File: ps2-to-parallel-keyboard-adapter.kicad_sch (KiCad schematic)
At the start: 7 parts, among them J1 PS/2 Keyboard Mini DIN 6, J2 Ferguson Keyboard Connector J2, U1 PIC16F84A, Y1 4 MHz

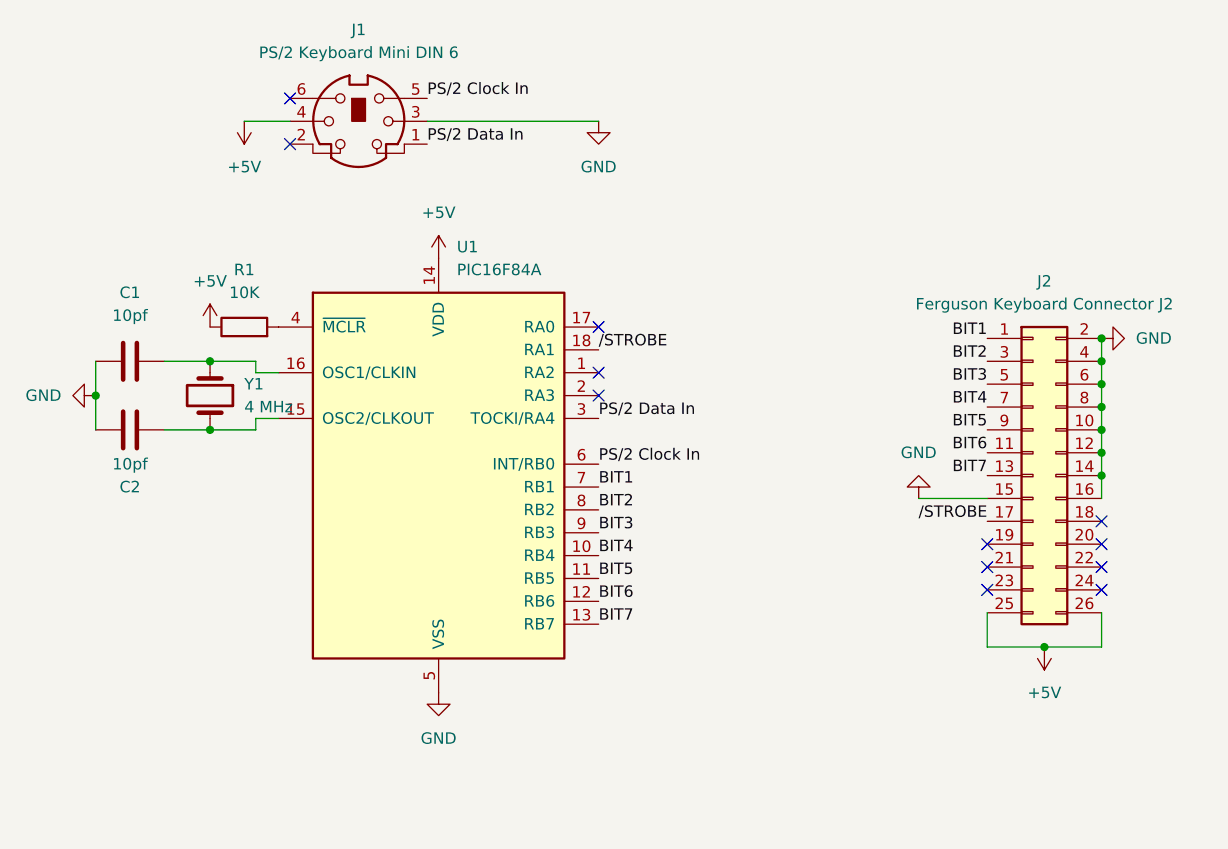
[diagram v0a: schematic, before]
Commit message: v1.1, add decoupling cap
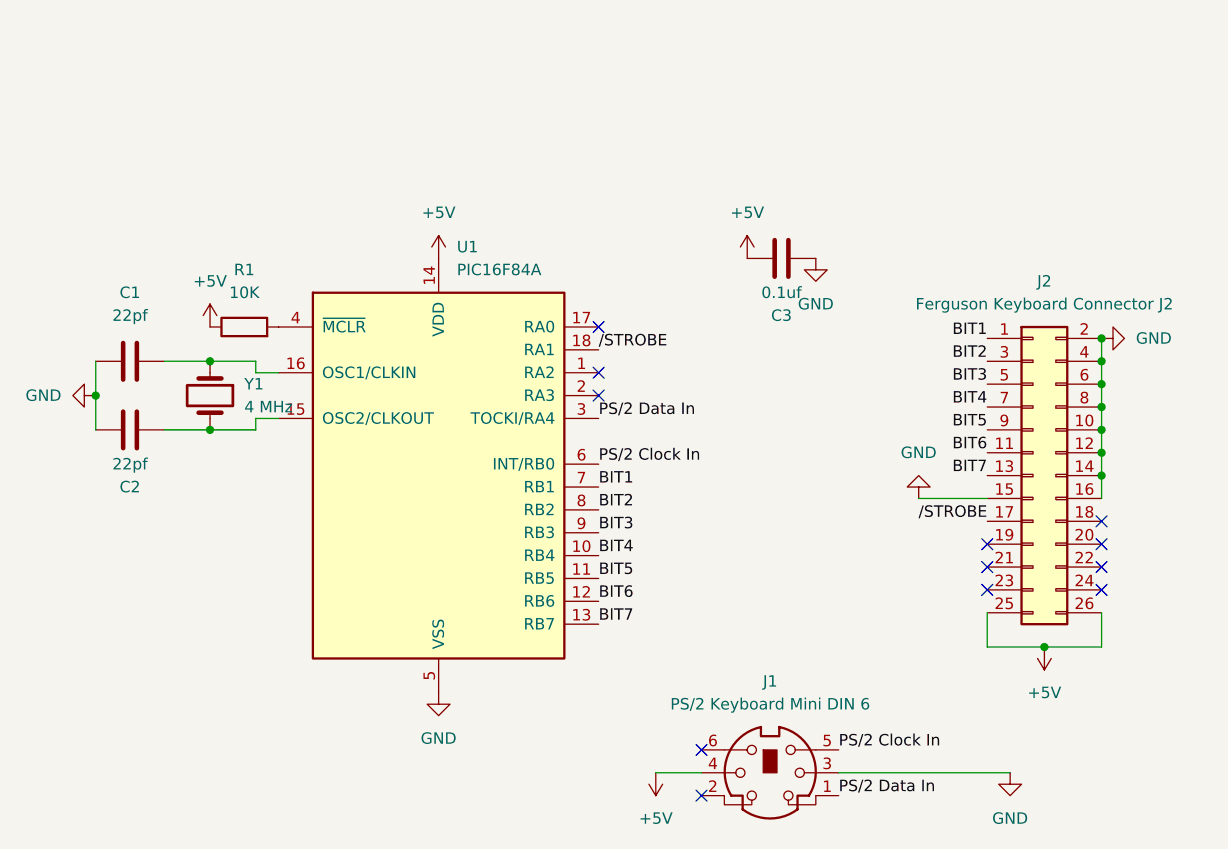
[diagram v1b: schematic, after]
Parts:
- added C3: 0.1uf, Capacitor_THT:C_Rect_L4.0mm_W2.5mm_P2.50mm, symbol Device:C
- C1, C2: value 10pf -> 22pf
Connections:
- net +5V: now also C3.1
- net GND: now also C3.2
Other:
- moved on the sheet: J1
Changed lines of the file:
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@@
   (no_connect (at 214.63 100.33))
   (no_connect (at 214.63 97.79))
-  (no_connect (at 137.16 53.34))
+  (no_connect (at 182.88 125.73))
   (no_connect (at 171.45 81.28))
   (no_connect (at 227.33 95.25))
@@
   (no_connect (at 227.33 102.87))
   (no_connect (at 227.33 97.79))
-  (no_connect (at 137.16 48.26))
+  (no_connect (at 182.88 120.65))
   (no_connect (at 171.45 73.66))
   (wire (pts (xy 133.35 85.09) (xy 128.27 85.09))
@@
     (stroke (width 0) (type default) (color 0 0 0 0))
   )
-  (wire (pts (xy 152.4 50.8) (xy 171.45 50.8))
+  (wire (pts (xy 198.12 123.19) (xy 217.17 123.19))
     (stroke (width 0) (type default) (color 0 0 0 0))
   )
@@
     (stroke (width 0) (type default) (color 0 0 0 0))
   )
-  (wire (pts (xy 132.08 50.8) (xy 137.16 50.8))
+  (wire (pts (xy 177.8 123.19) (xy 182.88 123.19))
     (stroke (width 0) (type default) (color 0 0 0 0))
   )
@@
     (effects (font (size 1.27 1.27)) (justify left bottom))
   )
-  (label "PS{slash}2 Clock In" (at 152.4 48.26 0)
+  (label "PS{slash}2 Clock In" (at 198.12 120.65 0)
     (effects (font (size 1.27 1.27)) (justify left bottom))
   )
@@
     (effects (font (size 1.27 1.27)) (justify right bottom))
   )
-  (label "PS{slash}2 Data In" (at 152.4 53.34 0)
+  (label "PS{slash}2 Data In" (at 198.12 125.73 0)
     (effects (font (size 1.27 1.27)) (justify left bottom))
   )
@@
     (pin "9")
   )
+  (symbol (lib_id "power:+5V") (at 187.96 66.04 0) (unit 1)
+    (in_bom yes) (on_board yes) (fields_autoplaced)
+    (property "Reference" "#PWR01" (id 0) (at 187.96 69.85 0)
+      (effects (font (size 1.27 1.27)) hide)
+    )
+    (property "Value" "+5V" (id 1) (at 187.96 60.96 0))
+    (property "Footprint" "" (id 2) (at 187.96 66.04 0)
+      (effects (font (size 1.27 1.27)) hide)
+    )
+    (property "Datasheet" "" (id 3) (at 187.96 66.04 0)
+      (effects (font (size 1.27 1.27)) hide)
+    )
+    (pin "1")
+  )
   (symbol (lib_id "Device:C") (at 119.38 85.09 90) (unit 1)
     (in_bom yes) (on_board yes)
     (property "Reference" "C2" (id 0) (at 119.38 91.44 90))
-    (property "Value" "10pf" (id 1) (at 119.38 88.9 90))
+    (property "Value" "22pf" (id 1) (at 119.38 88.9 90))
     (property "Footprint" "Capacitor_THT:C_Rect_L4.0mm_W2.5mm_P2.50mm" (id 2) (at 123.19 84.1248 0)
       (effects (font (size 1.27 1.27)) hide)
@@
     (pin "1")
   )
+  (symbol (lib_id "Device:C") (at 191.77 66.04 90) (unit 1)
+    (in_bom yes) (on_board yes)
+    (property "Reference" "C3" (id 0) (at 191.77 72.39 90))
+    (property "Value" "0.1uf" (id 1) (at 191.77 69.85 90))
+    (property "Footprint" "Capacitor_THT:C_Rect_L4.0mm_W2.5mm_P2.50mm" (id 2) (at 195.58 65.0748 0)
+      (effects (font (size 1.27 1.27)) hide)
+    )
+    (property "Datasheet" "~" (id 3) (at 191.77 66.04 0)
+      (effects (font (size 1.27 1.27)) hide)
+    )
+    (pin "1")
+    (pin "2")
+  )
   (symbol (lib_id "Device:C") (at 119.38 77.47 90) (unit 1)
     (in_bom yes) (on_board yes) (fields_autoplaced)
     (property "Reference" "C1" (id 0) (at 119.38 69.85 90))
-    (property "Value" "10pf" (id 1) (at 119.38 72.39 90))
+    (property "Value" "22pf" (id 1) (at 119.38 72.39 90))
     (property "Footprint" "Capacitor_THT:C_Rect_L4.0mm_W2.5mm_P2.50mm" (id 2) (at 123.19 76.5048 0)
       (effects (font (size 1.27 1.27)) hide)
@@
     (pin "9")
   )
-  (symbol (lib_id "Connector:Mini-DIN-6") (at 144.78 50.8 0) (unit 1)
-    (in_bom yes) (on_board yes) (fields_autoplaced)
-    (property "Reference" "J1" (id 0) (at 144.7977 40.64 0))
-    (property "Value" "PS/2 Keyboard Mini DIN 6" (id 1) (at 144.7977 43.18 0))
-    (property "Footprint" "SnapEDA Library:CUI_MD-60SM" (id 2) (at 144.78 50.8 0)
-      (effects (font (size 1.27 1.27)) hide)
-    )
-    (property "Datasheet" "http://service.powerdynamics.com/ec/Catalog17/Section%2011.pdf" (id 3) (at 144.78 50.8 0)
+  (symbol (lib_id "Connector:Mini-DIN-6") (at 190.5 123.19 0) (unit 1)
+    (in_bom yes) (on_board yes) (fields_autoplaced)
+    (property "Reference" "J1" (id 0) (at 190.5177 113.03 0))
+    (property "Value" "PS/2 Keyboard Mini DIN 6" (id 1) (at 190.5177 115.57 0))
+    (property "Footprint" "SnapEDA Library:CUI_MD-60SM" (id 2) (at 190.5 123.19 0)
+      (effects (font (size 1.27 1.27)) hide)
+    )
+    (property "Datasheet" "http://service.powerdynamics.com/ec/Catalog17/Section%2011.pdf" (id 3) (at 190.5 123.19 0)
       (effects (font (size 1.27 1.27)) hide)
     )
@@
     (pin "6")
   )
-  (symbol (lib_id "power:+5V") (at 132.08 50.8 180) (unit 1)
-    (in_bom yes) (on_board yes) (fields_autoplaced)
-    (property "Reference" "#PWR0105" (id 0) (at 132.08 46.99 0)
-      (effects (font (size 1.27 1.27)) hide)
-    )
-    (property "Value" "+5V" (id 1) (at 132.08 55.88 0))
-    (property "Footprint" "" (id 2) (at 132.08 50.8 0)
-      (effects (font (size 1.27 1.27)) hide)
-    )
-    (property "Datasheet" "" (id 3) (at 132.08 50.8 0)
+  (symbol (lib_id "power:+5V") (at 177.8 123.19 180) (unit 1)
+    (in_bom yes) (on_board yes) (fields_autoplaced)
+    (property "Reference" "#PWR0105" (id 0) (at 177.8 119.38 0)
+      (effects (font (size 1.27 1.27)) hide)
+    )
+    (property "Value" "+5V" (id 1) (at 177.8 128.27 0))
+    (property "Footprint" "" (id 2) (at 177.8 123.19 0)
+      (effects (font (size 1.27 1.27)) hide)
+    )
+    (property "Datasheet" "" (id 3) (at 177.8 123.19 0)
       (effects (font (size 1.27 1.27)) hide)
     )
@@
     (pin "1")
   )
-  (symbol (lib_id "power:GND") (at 171.45 50.8 0) (unit 1)
-    (in_bom yes) (on_board yes) (fields_autoplaced)
-    (property "Reference" "#PWR0103" (id 0) (at 171.45 57.15 0)
-      (effects (font (size 1.27 1.27)) hide)
-    )
-    (property "Value" "GND" (id 1) (at 171.45 55.88 0))
-    (property "Footprint" "" (id 2) (at 171.45 50.8 0)
-      (effects (font (size 1.27 1.27)) hide)
-    )
-    (property "Datasheet" "" (id 3) (at 171.45 50.8 0)
+  (symbol (lib_id "power:GND") (at 217.17 123.19 0) (unit 1)
+    (in_bom yes) (on_board yes) (fields_autoplaced)
+    (property "Reference" "#PWR0103" (id 0) (at 217.17 129.54 0)
+      (effects (font (size 1.27 1.27)) hide)
+    )
+    (property "Value" "GND" (id 1) (at 217.17 128.27 0))
+    (property "Footprint" "" (id 2) (at 217.17 123.19 0)
+      (effects (font (size 1.27 1.27)) hide)
+    )
+    (property "Datasheet" "" (id 3) (at 217.17 123.19 0)
       (effects (font (size 1.27 1.27)) hide)
     )
@@
     (pin "1")
   )
+  (symbol (lib_id "power:GND") (at 195.58 66.04 0) (unit 1)
+    (in_bom yes) (on_board yes) (fields_autoplaced)
+    (property "Reference" "#PWR02" (id 0) (at 195.58 72.39 0)
+      (effects (font (size 1.27 1.27)) hide)
+    )
+    (property "Value" "GND" (id 1) (at 195.58 71.12 0))
+    (property "Footprint" "" (id 2) (at 195.58 66.04 0)
+      (effects (font (size 1.27 1.27)) hide)
+    )
+    (property "Datasheet" "" (id 3) (at 195.58 66.04 0)
+      (effects (font (size 1.27 1.27)) hide)
+    )
+    (pin "1")
+  )
   (sheet_instances
     (path "/" (page "1"))
   )
   (symbol_instances
+    (path "/45eeee62-f84d-4442-a52b-ab85b2232f92"
+      (reference "#PWR01") (unit 1) (value "+5V") (footprint "")
+    )
+    (path "/f478c60c-f65a-426d-88b9-779e408ce9e4"
+      (reference "#PWR02") (unit 1) (value "GND") (footprint "")
+    )
     (path "/b4081ac5-e6ff-4b4a-8775-bffc53a5e4f4"
       (reference "#PWR0101") (unit 1) (value "+5V") (footprint "")
@@
     )
     (path "/62a3806b-64f3-4758-9c5f-b7bc2303f211"
-      (reference "C1") (unit 1) (value "10pf") (footprint "Capacitor_THT:C_Rect_L4.0mm_W2.5mm_P2.50mm")
+      (reference "C1") (unit 1) (value "22pf") (footprint "Capacitor_THT:C_Rect_L4.0mm_W2.5mm_P2.50mm")
     )
     (path "/476796b5-9101-4a52-b14d-b4de02a57d46"
-      (reference "C2") (unit 1) (value "10pf") (footprint "Capacitor_THT:C_Rect_L4.0mm_W2.5mm_P2.50mm")
+      (reference "C2") (unit 1) (value "22pf") (footprint "Capacitor_THT:C_Rect_L4.0mm_W2.5mm_P2.50mm")
+    )
+    (path "/50b724a6-f0e5-4131-9400-04acefa476be"
+      (reference "C3") (unit 1) (value "0.1uf") (footprint "Capacitor_THT:C_Rect_L4.0mm_W2.5mm_P2.50mm")
     )
     (path "/9cc9470d-be84-40a3-91ec-95264a7d868e"
